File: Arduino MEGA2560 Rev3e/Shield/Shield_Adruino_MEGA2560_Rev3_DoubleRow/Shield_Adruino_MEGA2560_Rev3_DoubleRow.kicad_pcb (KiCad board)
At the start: 2 copper layers, 101.6 x 53.3 mm, 16 parts

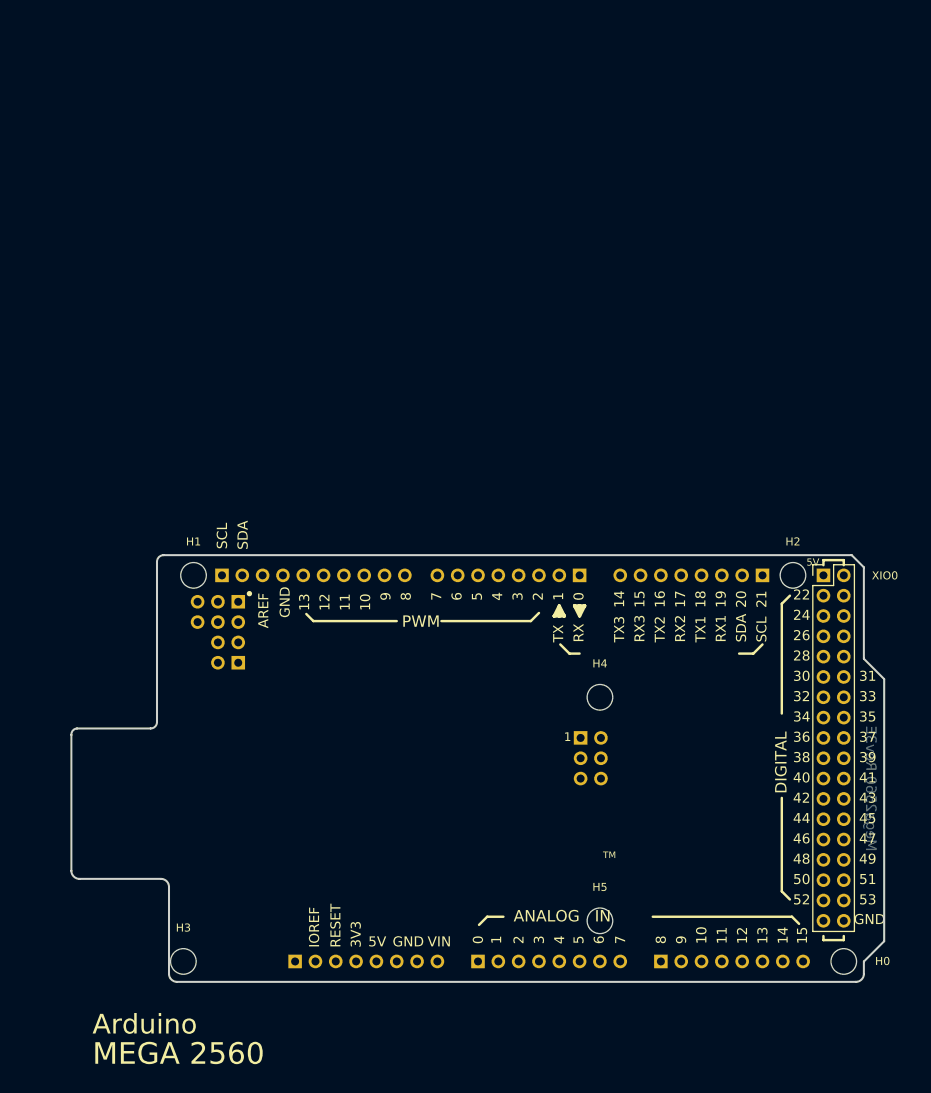
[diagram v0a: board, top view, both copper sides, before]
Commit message: REinstated IOREF
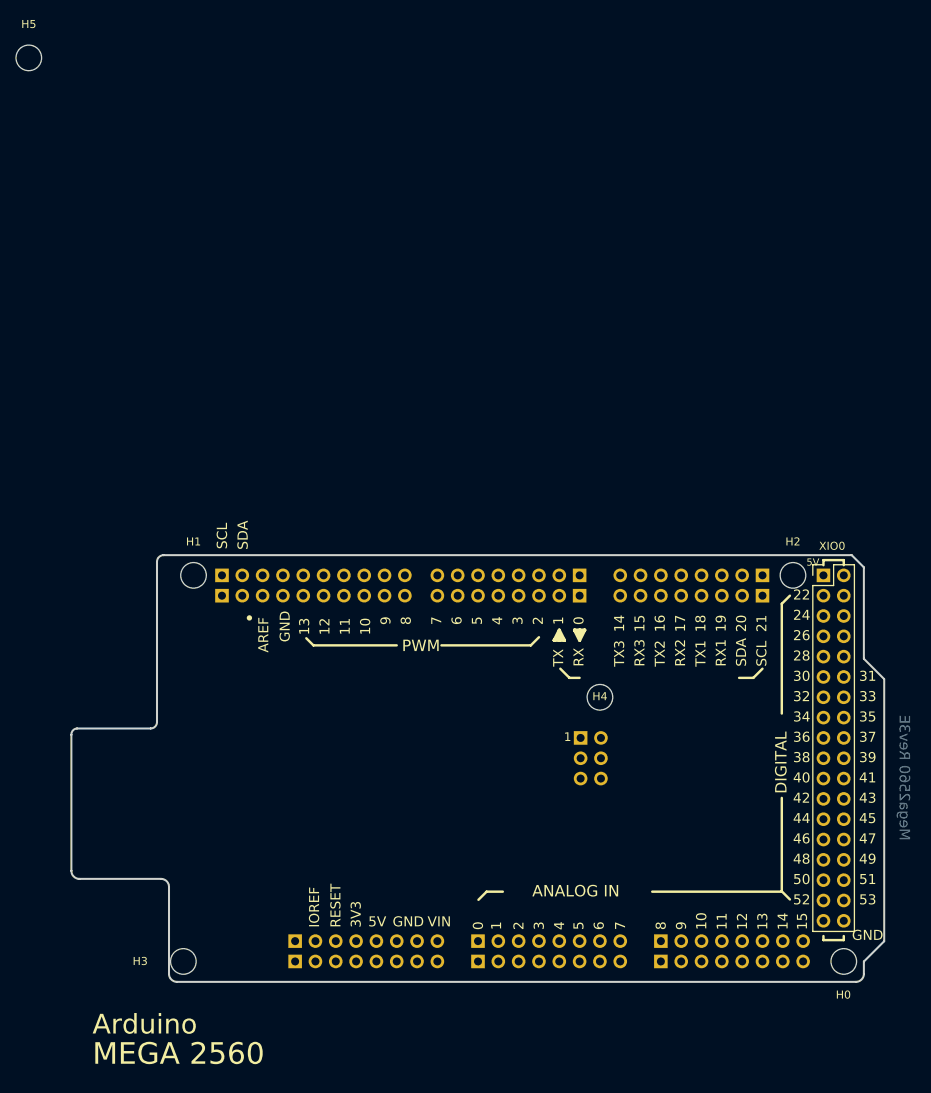
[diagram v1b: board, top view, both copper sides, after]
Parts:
- removed ICSP1: ICSP, Connector_PinSocket_2.54mm:PinSocket_2x03_P2.54mm_Vertical
- removed JP5: 2x2M - NM, Connector_PinSocket_2.54mm:PinSocket_2x02_P2.54mm_Vertical
- ADCH0, ADCL0, COMMUNICATION0, POWER0, PWML0: footprint Connector_PinHeader_2.54mm:PinHeader_1x08_P2.54mm_Vertical -> DoubleRows:PinHeader_1x08_P2.54mm_Vertical_Double
- JP6: footprint Connector_PinHeader_2.54mm:PinHeader_1x10_P2.54mm_Vertical -> DoubleRows:PinHeader_1x10_P2.54mm_Vertical_Double
- moved H5 129.4 mm to (92.4, 16.2)
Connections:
- net /RX1 renamed /RXD1
- net /RX2 renamed /RXD2
- net /RX3 renamed /RXD3
- net /TX1 renamed /TXD1
- net /TX2 renamed /TXD2
- net /TX3 renamed /TXD3
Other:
- board text removed: "TM"
